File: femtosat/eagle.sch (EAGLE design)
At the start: 6 parts, among them U1 ATMEGA328P_TQFP, U2 915MHz

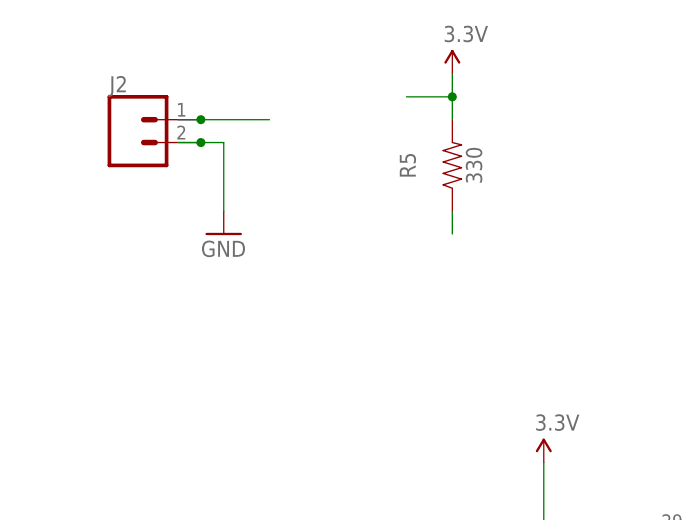
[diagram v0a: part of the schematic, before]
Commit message: Added to Battery Connector
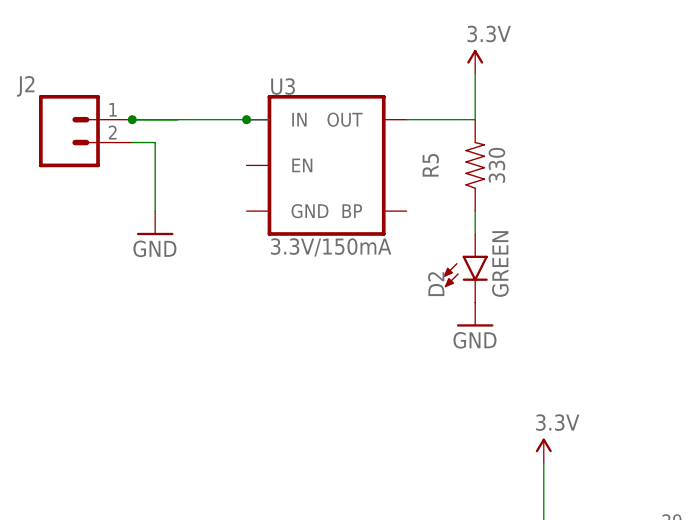
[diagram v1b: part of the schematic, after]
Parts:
- added D2: GREEN, femtosat:LED_GREEN0603
- added U3: 3.3V/150mA, femtosat:VOLTAGE_REGULATOR_MIC52053.3V
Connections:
- net 3.3V: now also U3.OUT
- net GND: now also D2.C
- net N$4: now also U3.IN
- net N$7: now also D2.A
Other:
- moved on the sheet: J2, R5
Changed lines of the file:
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@@
 <part name="R5" library="femtosat" deviceset="RESISTOR_330OHM" device="-0603-1/10W-1%" value="330"/>
 <part name="J2" library="femtosat" deviceset="CONNECTOR_2PIN" device="-JST-2MM-SMT"/>
+<part name="D2" library="femtosat" deviceset="LED_GREEN" device="0603" value="GREEN"/>
+<part name="GND4" library="femtosat" deviceset="GND" device=""/>
+<part name="U3" library="femtosat" deviceset="VOLTAGE_REGULATOR_MIC5205" device="3.3V" value="3.3V/150mA"/>
 </parts>
 <sheets>
@@
 <attribute name="NAME" x="43.18" y="127.762" size="1.778" layer="95"/>
 </instance>
-<instance part="GND3" gate="1" x="58.42" y="172.72" smashed="yes">
-<attribute name="VALUE" x="55.88" y="170.18" size="1.778" layer="96"/>
-</instance>
-<instance part="P+3" gate="G$1" x="83.82" y="190.5" smashed="yes">
-<attribute name="VALUE" x="82.804" y="194.056" size="1.778" layer="96"/>
-</instance>
-<instance part="R5" gate="G$1" x="83.82" y="180.34" smashed="yes" rot="R90">
-<attribute name="NAME" x="79.756" y="180.34" size="1.778" layer="95" font="vector" rot="R90" align="bottom-center"/>
-<attribute name="VALUE" x="85.344" y="180.34" size="1.778" layer="96" font="vector" rot="R90" align="top-center"/>
-</instance>
-<instance part="J2" gate="G$1" x="48.26" y="182.88" smashed="yes">
-<attribute name="VALUE" x="45.72" y="178.054" size="1.778" layer="96" font="vector"/>
-<attribute name="NAME" x="45.72" y="188.468" size="1.778" layer="95" font="vector"/>
+<instance part="GND3" gate="1" x="50.8" y="172.72" smashed="yes">
+<attribute name="VALUE" x="48.26" y="170.18" size="1.778" layer="96"/>
+</instance>
+<instance part="P+3" gate="G$1" x="86.36" y="190.5" smashed="yes">
+<attribute name="VALUE" x="85.344" y="194.056" size="1.778" layer="96"/>
+</instance>
+<instance part="R5" gate="G$1" x="86.36" y="180.34" smashed="yes" rot="R90">
+<attribute name="NAME" x="82.296" y="180.34" size="1.778" layer="95" font="vector" rot="R90" align="bottom-center"/>
+<attribute name="VALUE" x="87.884" y="180.34" size="1.778" layer="96" font="vector" rot="R90" align="top-center"/>
+</instance>
+<instance part="J2" gate="G$1" x="40.64" y="182.88" smashed="yes">
+<attribute name="VALUE" x="38.1" y="178.054" size="1.778" layer="96" font="vector"/>
+<attribute name="NAME" x="35.56" y="188.468" size="1.778" layer="95" font="vector"/>
+</instance>
+<instance part="D2" gate="G$1" x="86.36" y="170.18" smashed="yes">
+<attribute name="NAME" x="82.931" y="165.608" size="1.778" layer="95" font="vector" rot="R90"/>
+<attribute name="VALUE" x="88.265" y="165.608" size="1.778" layer="96" font="vector" rot="R90" align="top-left"/>
+</instance>
+<instance part="GND4" gate="1" x="86.36" y="162.56" smashed="yes">
+<attribute name="VALUE" x="83.82" y="160.02" size="1.778" layer="96"/>
+</instance>
+<instance part="U3" gate="U1" x="71.12" y="180.34" smashed="yes">
+<attribute name="NAME" x="63.5" y="188.214" size="1.778" layer="95" font="vector"/>
+<attribute name="VALUE" x="63.5" y="172.212" size="1.778" layer="96" font="vector" align="top-left"/>
 </instance>
 </instances>
@@
 </segment>
 <segment>
-<wire x1="53.34" y1="182.88" x2="55.88" y2="182.88" width="0.1524" layer="91"/>
-<wire x1="55.88" y1="182.88" x2="58.42" y2="182.88" width="0.1524" layer="91"/>
-<wire x1="58.42" y1="182.88" x2="58.42" y2="175.26" width="0.1524" layer="91"/>
+<wire x1="48.26" y1="182.88" x2="50.8" y2="182.88" width="0.1524" layer="91"/>
+<wire x1="50.8" y1="182.88" x2="50.8" y2="175.26" width="0.1524" layer="91"/>
 <pinref part="GND3" gate="1" pin="GND"/>
 <pinref part="J2" gate="G$1" pin="2"/>
-<junction x="55.88" y="182.88"/>
+</segment>
+<segment>
+<pinref part="D2" gate="G$1" pin="C"/>
+<pinref part="GND4" gate="1" pin="GND"/>
 </segment>
 </net>
@@
 <segment>
 <pinref part="P+3" gate="G$1" pin="3.3V"/>
-<wire x1="83.82" y1="190.5" x2="83.82" y2="187.96" width="0.1524" layer="91"/>
-<wire x1="83.82" y1="187.96" x2="78.74" y2="187.96" width="0.1524" layer="91"/>
-<wire x1="83.82" y1="185.42" x2="83.82" y2="187.96" width="0.1524" layer="91"/>
-<junction x="83.82" y="187.96"/>
+<wire x1="86.36" y1="190.5" x2="86.36" y2="185.42" width="0.1524" layer="91"/>
+<wire x1="86.36" y1="185.42" x2="78.74" y2="185.42" width="0.1524" layer="91"/>
 <pinref part="R5" gate="G$1" pin="2"/>
+<pinref part="U3" gate="U1" pin="OUT"/>
 </segment>
 </net>
@@
 <net name="N$4" class="0">
 <segment>
-<wire x1="53.34" y1="185.42" x2="55.88" y2="185.42" width="0.1524" layer="91"/>
+<wire x1="53.34" y1="185.42" x2="48.26" y2="185.42" width="0.1524" layer="91"/>
 <pinref part="J2" gate="G$1" pin="1"/>
-<wire x1="55.88" y1="185.42" x2="63.5" y2="185.42" width="0.1524" layer="91"/>
-<junction x="55.88" y="185.42"/>
+<wire x1="48.26" y1="185.42" x2="60.96" y2="185.42" width="0.1524" layer="91"/>
+<junction x="48.26" y="185.42"/>
+<pinref part="U3" gate="U1" pin="IN"/>
+<wire x1="60.96" y1="185.42" x2="63.5" y2="185.42" width="0.1524" layer="91"/>
+<junction x="60.96" y="185.42"/>
 </segment>
 </net>
@@
 <segment>
 <pinref part="R5" gate="G$1" pin="1"/>
-<wire x1="83.82" y1="175.26" x2="83.82" y2="172.72" width="0.1524" layer="91"/>
-</segment>
-</net>
+<wire x1="86.36" y1="175.26" x2="86.36" y2="172.72" width="0.1524" layer="91"/>
+<pinref part="D2" gate="G$1" pin="A"/>
+</segment>
+</net>

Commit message: Finished Battery Connector
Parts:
- added C1, C2: 1.0uF, femtosat:CAPACITOR_1.0UF-0603-16V-10%
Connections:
- new net N$9: C1.1, U3.BP
- net 3.3V: now also C2.2
- net GND: now also C1.2, C2.1, J2.1, U3.GND; no longer J2.2
- net N$4: now also J2.2, U3.EN; no longer J2.1
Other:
- moved on the sheet: J2
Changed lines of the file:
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@@
 <part name="P+3" library="femtosat" deviceset="3.3V" device=""/>
 <part name="R5" library="femtosat" deviceset="RESISTOR_330OHM" device="-0603-1/10W-1%" value="330"/>
-<part name="J2" library="femtosat" deviceset="CONNECTOR_2PIN" device="-JST-2MM-SMT"/>
 <part name="D2" library="femtosat" deviceset="LED_GREEN" device="0603" value="GREEN"/>
 <part name="GND4" library="femtosat" deviceset="GND" device=""/>
 <part name="U3" library="femtosat" deviceset="VOLTAGE_REGULATOR_MIC5205" device="3.3V" value="3.3V/150mA"/>
+<part name="C1" library="femtosat" deviceset="CAPACITOR_1.0UF" device="-0603-16V-10%" value="1.0uF"/>
+<part name="J2" library="femtosat" deviceset="CONNECTOR_2PIN" device="-JST-2MM-SMT"/>
+<part name="C2" library="femtosat" deviceset="CAPACITOR_1.0UF" device="-0603-16V-10%" value="1.0uF"/>
+<part name="GND5" library="femtosat" deviceset="GND" device=""/>
 </parts>
 <sheets>
@@
 <attribute name="VALUE" x="87.884" y="180.34" size="1.778" layer="96" font="vector" rot="R90" align="top-center"/>
 </instance>
-<instance part="J2" gate="G$1" x="40.64" y="182.88" smashed="yes">
-<attribute name="VALUE" x="38.1" y="178.054" size="1.778" layer="96" font="vector"/>
-<attribute name="NAME" x="35.56" y="188.468" size="1.778" layer="95" font="vector"/>
-</instance>
 <instance part="D2" gate="G$1" x="86.36" y="170.18" smashed="yes">
 <attribute name="NAME" x="82.931" y="165.608" size="1.778" layer="95" font="vector" rot="R90"/>
@@
 <attribute name="NAME" x="63.5" y="188.214" size="1.778" layer="95" font="vector"/>
 <attribute name="VALUE" x="63.5" y="172.212" size="1.778" layer="96" font="vector" align="top-left"/>
+</instance>
+<instance part="C1" gate="G$1" x="68.58" y="165.1" smashed="yes" rot="R270">
+<attribute name="NAME" x="71.501" y="163.576" size="1.778" layer="95" font="vector" rot="R270"/>
+<attribute name="VALUE" x="66.421" y="163.576" size="1.778" layer="96" font="vector" rot="R270"/>
+</instance>
+<instance part="J2" gate="G$1" x="40.64" y="185.42" smashed="yes">
+<attribute name="VALUE" x="38.1" y="180.594" size="1.778" layer="96" font="vector"/>
+<attribute name="NAME" x="38.1" y="191.008" size="1.778" layer="95" font="vector"/>
+</instance>
+<instance part="C2" gate="G$1" x="96.52" y="185.42" smashed="yes" rot="R270">
+<attribute name="NAME" x="99.441" y="183.896" size="1.778" layer="95" font="vector" rot="R270"/>
+<attribute name="VALUE" x="94.361" y="183.896" size="1.778" layer="96" font="vector" rot="R270"/>
+</instance>
+<instance part="GND5" gate="1" x="104.14" y="185.42" smashed="yes" rot="R90">
+<attribute name="VALUE" x="106.68" y="182.88" size="1.778" layer="96" rot="R90"/>
 </instance>
 </instances>
@@
 </segment>
 <segment>
-<wire x1="48.26" y1="182.88" x2="50.8" y2="182.88" width="0.1524" layer="91"/>
-<wire x1="50.8" y1="182.88" x2="50.8" y2="175.26" width="0.1524" layer="91"/>
+<wire x1="50.8" y1="187.96" x2="50.8" y2="175.26" width="0.1524" layer="91"/>
 <pinref part="GND3" gate="1" pin="GND"/>
-<pinref part="J2" gate="G$1" pin="2"/>
+<pinref part="U3" gate="U1" pin="GND"/>
+<wire x1="60.96" y1="175.26" x2="50.8" y2="175.26" width="0.1524" layer="91"/>
+<wire x1="60.96" y1="175.26" x2="60.96" y2="165.1" width="0.1524" layer="91"/>
+<junction x="60.96" y="175.26"/>
+<wire x1="60.96" y1="165.1" x2="66.04" y2="165.1" width="0.1524" layer="91"/>
+<pinref part="C1" gate="G$1" pin="2"/>
+<pinref part="J2" gate="G$1" pin="1"/>
+<wire x1="48.26" y1="187.96" x2="50.8" y2="187.96" width="0.1524" layer="91"/>
 </segment>
 <segment>
 <pinref part="D2" gate="G$1" pin="C"/>
 <pinref part="GND4" gate="1" pin="GND"/>
+</segment>
+<segment>
+<pinref part="C2" gate="G$1" pin="1"/>
+<pinref part="GND5" gate="1" pin="GND"/>
 </segment>
 </net>
@@
 <pinref part="R5" gate="G$1" pin="2"/>
 <pinref part="U3" gate="U1" pin="OUT"/>
+<wire x1="86.36" y1="185.42" x2="93.98" y2="185.42" width="0.1524" layer="91"/>
+<junction x="86.36" y="185.42"/>
+<pinref part="C2" gate="G$1" pin="2"/>
 </segment>
 </net>
@@
 <net name="N$4" class="0">
 <segment>
-<wire x1="53.34" y1="185.42" x2="48.26" y2="185.42" width="0.1524" layer="91"/>
-<pinref part="J2" gate="G$1" pin="1"/>
-<wire x1="48.26" y1="185.42" x2="60.96" y2="185.42" width="0.1524" layer="91"/>
-<junction x="48.26" y="185.42"/>
 <pinref part="U3" gate="U1" pin="IN"/>
 <wire x1="60.96" y1="185.42" x2="63.5" y2="185.42" width="0.1524" layer="91"/>
 <junction x="60.96" y="185.42"/>
+<pinref part="U3" gate="U1" pin="EN"/>
+<wire x1="60.96" y1="180.34" x2="60.96" y2="185.42" width="0.1524" layer="91"/>
+<pinref part="J2" gate="G$1" pin="2"/>
+<wire x1="48.26" y1="185.42" x2="60.96" y2="185.42" width="0.1524" layer="91"/>
 </segment>
 </net>
@@
 </segment>
 </net>
+<net name="N$9" class="0">
+<segment>
+<pinref part="U3" gate="U1" pin="BP"/>
+<wire x1="78.74" y1="175.26" x2="78.74" y2="165.1" width="0.1524" layer="91"/>
+<wire x1="78.74" y1="165.1" x2="73.66" y2="165.1" width="0.1524" layer="91"/>
+<pinref part="C1" gate="G$1" pin="1"/>
+</segment>
+</net>

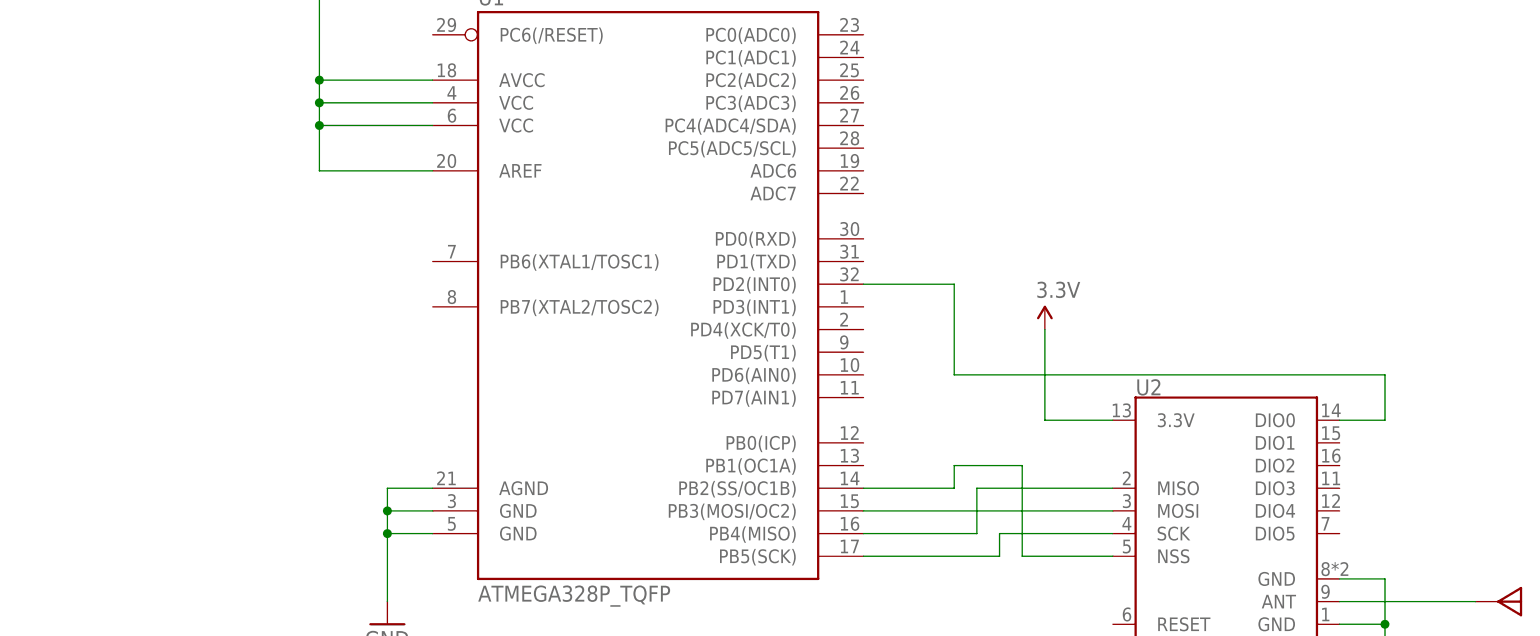
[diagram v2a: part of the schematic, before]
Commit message: Added Clock and LED
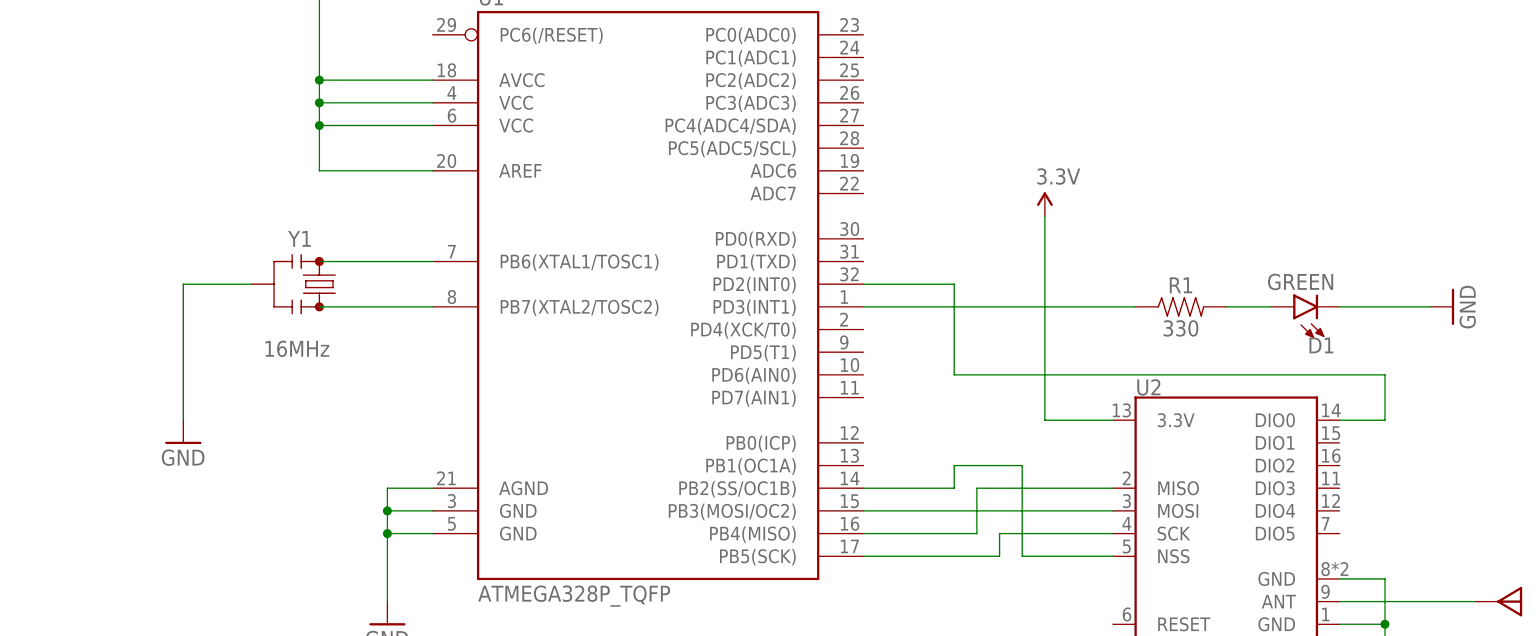
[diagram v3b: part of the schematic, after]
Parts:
- added D1: GREEN, femtosat:LED_GREEN0603
- added R1: 330, femtosat:RESISTOR_330OHM-0603-1/10W-1%
- added Y1: 16MHz, femtosat:RESONATOR_16MHZSMD_3.2X1.3
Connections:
- new net N$10: U1.PB6(XTAL1/TOSC1), Y1.1
- new net N$11: U1.PB7(XTAL2/TOSC2), Y1.3
- new net N$12: D1.A, R1.2
- new net N$13: R1.1, U1.PD3(INT1)
- net GND: now also D1.C, Y1.2
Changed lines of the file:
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@@
 <setting verticaltext="up"/>
 </settings>
-<grid distance="0.1" unitdist="inch" unit="inch" style="lines" multiple="1" display="no" altdistance="0.01" altunitdist="inch" altunit="inch"/>
+<grid distance="0.1" unitdist="inch" unit="inch" style="lines" multiple="1" display="yes" altdistance="0.01" altunitdist="inch" altunit="inch"/>
 <layers>
 <layer number="1" name="Top" color="4" fill="1" visible="no" active="no"/>
@@
 <part name="C2" library="femtosat" deviceset="CAPACITOR_1.0UF" device="-0603-16V-10%" value="1.0uF"/>
 <part name="GND5" library="femtosat" deviceset="GND" device=""/>
+<part name="Y1" library="femtosat" deviceset="RESONATOR_16MHZ" device="SMD_3.2X1.3" value="16MHz"/>
+<part name="GND6" library="femtosat" deviceset="GND" device=""/>
+<part name="R1" library="femtosat" deviceset="RESISTOR_330OHM" device="-0603-1/10W-1%" value="330"/>
+<part name="D1" library="femtosat" deviceset="LED_GREEN" device="0603" value="GREEN"/>
+<part name="GND7" library="femtosat" deviceset="GND" device=""/>
 </parts>
 <sheets>
@@
 </instance>
 <instance part="ANT1" gate="G$1" x="228.6" y="76.2" smashed="yes"/>
-<instance part="P+1" gate="G$1" x="175.26" y="106.68" smashed="yes">
-<attribute name="VALUE" x="174.244" y="110.236" size="1.778" layer="96"/>
+<instance part="P+1" gate="G$1" x="175.26" y="119.38" smashed="yes">
+<attribute name="VALUE" x="174.244" y="122.936" size="1.778" layer="96"/>
 </instance>
 <instance part="GND2" gate="1" x="101.6" y="73.66" smashed="yes">
@@
 <instance part="GND5" gate="1" x="104.14" y="185.42" smashed="yes" rot="R90">
 <attribute name="VALUE" x="106.68" y="182.88" size="1.778" layer="96" rot="R90"/>
+</instance>
+<instance part="Y1" gate="G$1" x="93.98" y="111.76" smashed="yes" rot="R270">
+<attribute name="NAME" x="93.218" y="116.84" size="1.778" layer="95" font="vector" align="center-right"/>
+<attribute name="VALUE" x="91.44" y="103.632" size="1.778" layer="96" font="vector" align="bottom-center"/>
+</instance>
+<instance part="GND6" gate="1" x="78.74" y="93.98" smashed="yes">
+<attribute name="VALUE" x="76.2" y="91.44" size="1.778" layer="96"/>
+</instance>
+<instance part="R1" gate="G$1" x="190.5" y="109.22" smashed="yes">
+<attribute name="NAME" x="190.5" y="110.744" size="1.778" layer="95" font="vector" align="bottom-center"/>
+<attribute name="VALUE" x="190.5" y="107.696" size="1.778" layer="96" font="vector" align="top-center"/>
+</instance>
+<instance part="D1" gate="G$1" x="203.2" y="109.22" smashed="yes" rot="R90">
+<attribute name="NAME" x="207.772" y="105.791" size="1.778" layer="95" font="vector" rot="R180"/>
+<attribute name="VALUE" x="207.772" y="111.125" size="1.778" layer="96" font="vector" rot="R180" align="top-left"/>
+</instance>
+<instance part="GND7" gate="1" x="220.98" y="109.22" smashed="yes" rot="R90">
+<attribute name="VALUE" x="223.52" y="106.68" size="1.778" layer="96" rot="R90"/>
 </instance>
 </instances>
@@
 <pinref part="GND5" gate="1" pin="GND"/>
 </segment>
+<segment>
+<pinref part="Y1" gate="G$1" pin="2"/>
+<wire x1="86.36" y1="111.76" x2="78.74" y2="111.76" width="0.1524" layer="91"/>
+<wire x1="78.74" y1="111.76" x2="78.74" y2="96.52" width="0.1524" layer="91"/>
+<pinref part="GND6" gate="1" pin="GND"/>
+</segment>
+<segment>
+<pinref part="D1" gate="G$1" pin="C"/>
+<wire x1="208.28" y1="109.22" x2="218.44" y2="109.22" width="0.1524" layer="91"/>
+<pinref part="GND7" gate="1" pin="GND"/>
+</segment>
 </net>
 <net name="N$5" class="0">
@@
 <pinref part="U2" gate="G$1" pin="3.3V"/>
 <wire x1="182.88" y1="96.52" x2="175.26" y2="96.52" width="0.1524" layer="91"/>
-<wire x1="175.26" y1="96.52" x2="175.26" y2="106.68" width="0.1524" layer="91"/>
+<wire x1="175.26" y1="96.52" x2="175.26" y2="119.38" width="0.1524" layer="91"/>
 <pinref part="P+1" gate="G$1" pin="3.3V"/>
 </segment>
@@
 </segment>
 </net>
+<net name="N$10" class="0">
+<segment>
+<pinref part="U1" gate="U$1" pin="PB6(XTAL1/TOSC1)"/>
+<pinref part="Y1" gate="G$1" pin="1"/>
+<wire x1="106.68" y1="114.3" x2="93.98" y2="114.3" width="0.1524" layer="91"/>
+</segment>
+</net>
+<net name="N$11" class="0">
+<segment>
+<pinref part="U1" gate="U$1" pin="PB7(XTAL2/TOSC2)"/>
+<pinref part="Y1" gate="G$1" pin="3"/>
+<wire x1="106.68" y1="109.22" x2="93.98" y2="109.22" width="0.1524" layer="91"/>
+</segment>
+</net>
+<net name="N$13" class="0">
+<segment>
+<pinref part="U1" gate="U$1" pin="PD3(INT1)"/>
+<wire x1="154.94" y1="109.22" x2="185.42" y2="109.22" width="0.1524" layer="91"/>
+<pinref part="R1" gate="G$1" pin="1"/>
+</segment>
+</net>
+<net name="N$12" class="0">
+<segment>
+<pinref part="R1" gate="G$1" pin="2"/>
+<wire x1="195.58" y1="109.22" x2="200.66" y2="109.22" width="0.1524" layer="91"/>
+<pinref part="D1" gate="G$1" pin="A"/>
+</segment>
+</net>
